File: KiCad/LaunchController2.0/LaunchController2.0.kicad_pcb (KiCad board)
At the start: 2 copper layers, 150 x 100 mm, 182 parts, among them J1 CONN_ICSP, J10 CONN_PANEL_BOARD_2, J11 CONN_AUDIO, J12 CONN_SPEAKER, J13 CONN_RS485, J2 CONN_USB, J3 USB_C_Receptacle_USB2.0_16P, J4 TO_CONVERTER, J5 FROM_CONVERTER, J6 DC_IN, J7 CONN_STATUS_PANEL, J8 CONN_BOARD_3, J9 CONN_PANEL_BOARD_1, Q1 TJ8S06M3L, Q2 2SC3325-Y, Q3 TJ8S06M3L, SW1 SW_Push, SW10 SW_Push, SW11 SW_Push, SW12 SW_Push, SW13 SW_Push, SW14 SW_Push, SW15 SW_Push, SW16 SW_Push, SW17 SW_Push, SW2 SW_Push, SW3 SW_Push, SW4 SW_Push, SW5 SW_Push, SW6 SW_Push, SW7 SW_Push, SW8 SW_Push, SW9 SW_Push, U1 ATmega2560-16A, U10 ADM2582E, U11 24LC256, U2 FT232RNL, U3 USBLC6-2SC6, U4 TPS2116DRL, U5 NJM7805SDL1, U6 INA219BIDCNT, U7 INA219BIDCNT, U9 DFPlayer, Y1 HUSG-16.000-20

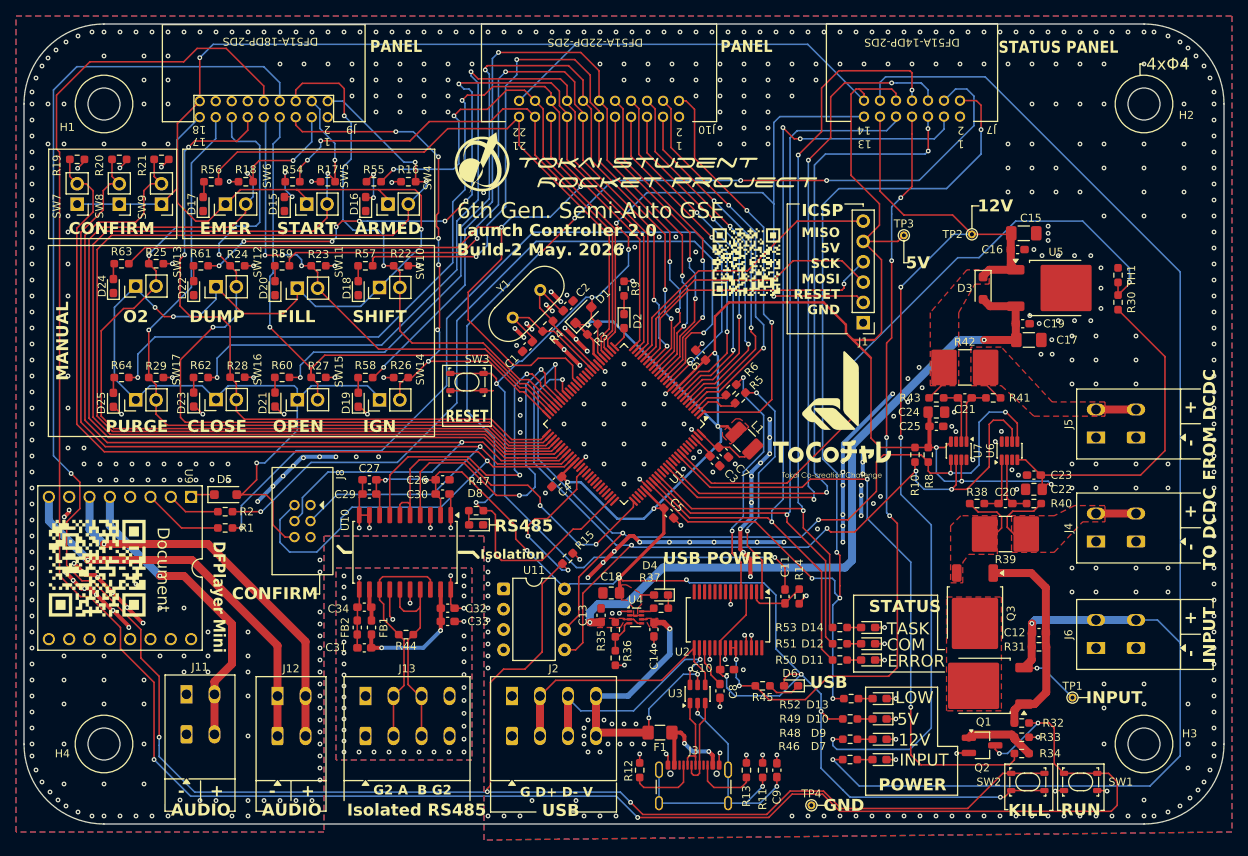
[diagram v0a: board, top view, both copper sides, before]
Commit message: シルクなどを調整
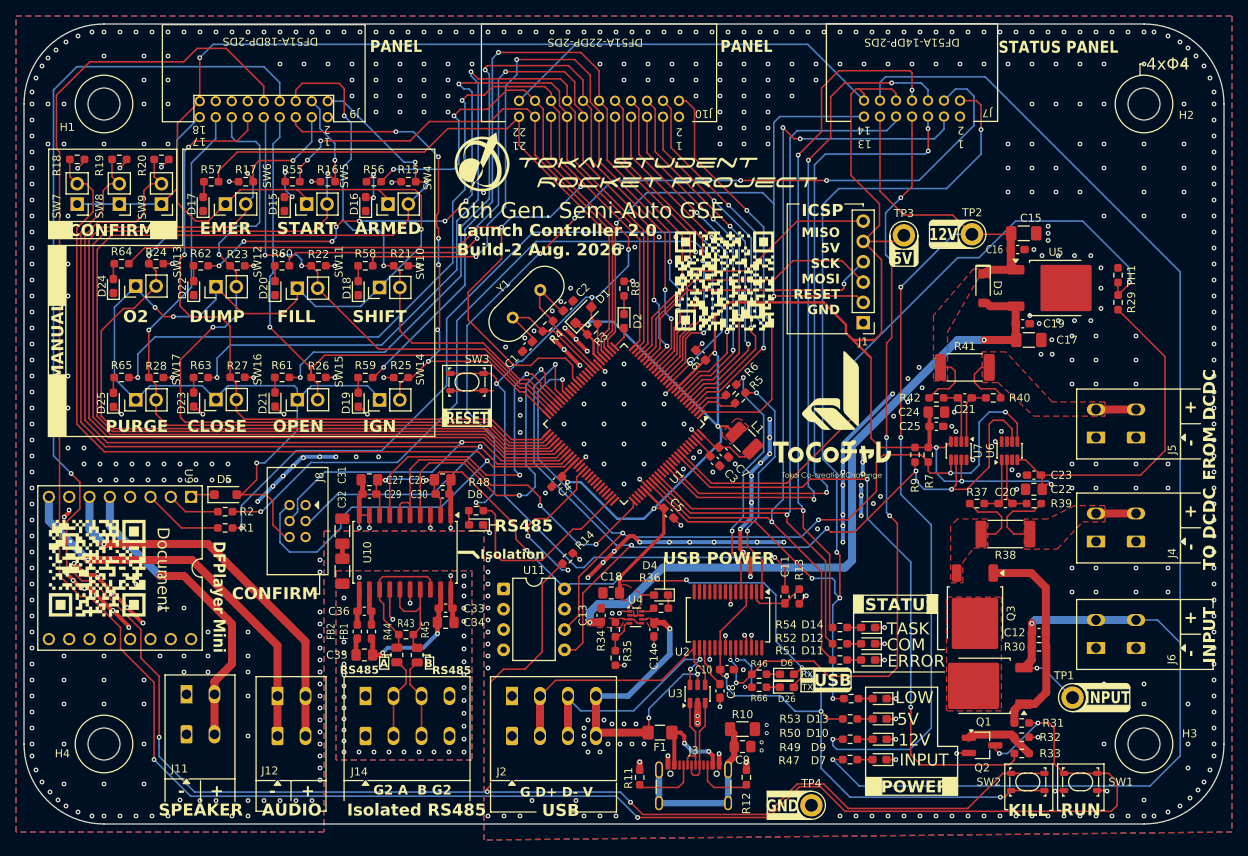
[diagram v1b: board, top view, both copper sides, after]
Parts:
- added C31: 470pF, Capacitor_SMD:C_1206_3216Metric_Pad1.33x1.80mm_HandSolder, F.Cu at (115.8, 114.4)
- added C32: 470pF, Capacitor_SMD:C_1206_3216Metric_Pad1.33x1.80mm_HandSolder, F.Cu at (115.8, 119.4)
- added D26: LED_O, LED_SMD:LED_0603_1608Metric_Pad1.05x0.95mm_HandSolder, F.Cu at (171.3, 133.9)
- added R44: TestPoint_A, Resistor_SMD:R_0805_2012Metric, F.Cu at (122.6, 129.9)
- added R45: TestPoint_B, Resistor_SMD:R_0805_2012Metric, F.Cu at (125.1, 129.9)
- added R66: 1kR, Resistor_SMD:R_0603_1608Metric_Pad0.98x0.95mm_HandSolder, F.Cu at (167.9, 133.9)
- C20, C21: value uF -> 0.1uF
- C26, C27: value 0.1uF -> 10uF; footprint Capacitor_SMD:C_0603_1608Metric_Pad1.08x0.95mm_HandSolder -> Capacitor_SMD:C_0805_2012Metric_Pad1.18x1.45mm_HandSolder
- C29, C30: value 0.01uF -> 0.1uF
- C34: renamed from C32; value 0.01uF -> 10uF; footprint Capacitor_SMD:C_0603_1608Metric_Pad1.08x0.95mm_HandSolder -> Capacitor_SMD:C_0805_2012Metric_Pad1.18x1.45mm_HandSolder
- C35: renamed from C34; value 0.01uF -> 10uF; footprint Capacitor_SMD:C_0603_1608Metric_Pad1.08x0.95mm_HandSolder -> Capacitor_SMD:C_0805_2012Metric_Pad1.18x1.45mm_HandSolder
- C9: value 4.7uF -> 10nF; footprint Capacitor_SMD:C_0603_1608Metric_Pad1.08x0.95mm_HandSolder -> Capacitor_SMD:C_0805_2012Metric_Pad1.18x1.45mm_HandSolder
- D3: value GS1010FL -> SS2040FL; footprint Diode_SMD:D_SOD-123F -> TSRP_Diode:SOD-123FL_Handsolder
- D6: value LED_B -> LED_G
- R10: renamed from R11; footprint Resistor_SMD:R_0603_1608Metric_Pad0.98x0.95mm_HandSolder -> Resistor_SMD:R_1206_3216Metric_Pad1.30x1.75mm_HandSolder
- R36: renamed from R37; value 100 -> 100R
- R37: renamed from R38; value 0R -> 10R
- R38: renamed from R39; footprint Resistor_SMD:R_2816_7142Metric_Pad3.20x4.45mm_HandSolder -> Resistor_SMD:R_2512_6332Metric_Pad1.40x3.35mm_HandSolder
- R39: renamed from R40; value 0R -> 10R
- R40: renamed from R41; value 0R -> 10R
- R41: renamed from R42; footprint Resistor_SMD:R_2816_7142Metric_Pad3.20x4.45mm_HandSolder -> Resistor_SMD:R_2512_6332Metric_Pad1.40x3.35mm_HandSolder
- R42: renamed from R43; value 0R -> 10R
- TP1, TP2, TP3, TP4: footprint TestPoint:TestPoint_THTPad_D1.0mm_Drill0.5mm -> TestPoint:TestPoint_Keystone_5005-5009_Compact
- U10: value ADM2582E -> ADM2587EBRWZ
- moved C33 11.3 mm to (128.7, 124.0), turned to 180 degrees
- moved C36 10.5 mm to (118.5, 124.4), turned to 0 degrees
- moved C35 5.97 mm to (118.5, 129.9)
- moved R10 5.72 mm to (165.8, 139.1), turned to 0 degrees
- moved C9 5.21 mm to (165.8, 141.3), turned to 180 degrees
- moved G*** 3.62 mm to (163.6, 83.1)
- moved C34 1.80 mm to (128.7, 125.8)
- moved D6 1.54 mm to (171.4, 132.3), turned to 0 degrees
- moved R46 1.51 mm to (167.9, 132.3)
- moved R11 0.91 mm to (153.0, 145.2)
- moved R12 0.91 mm to (166.3, 145.2)
- moved J8 0.61 mm to (113.8, 113.1)
- moved FB1 0.51 mm to (119.4, 126.9)
- moved FB2 0.51 mm to (117.7, 126.9)
- renumbered C31 to C33, C33 to C36, J13 to J14, R12 to R11, R13 to R12, R14 to R13, R15 to R14, R16 to R15, R17 to R16, R18 to R17, R19 to R18, R20 to R19, R21 to R20, R22 to R21, R23 to R22, R24 to R23, R25 to R24, R26 to R25, R27 to R26, R28 to R27, R29 to R28, R30 to R29, R31 to R30, R32 to R31, R33 to R32, R34 to R33, R35 to R34, R36 to R35, R44 to R43, R45 to R46, R46 to R47, R47 to R48, R48 to R49, R49 to R50, R50 to R51, R51 to R52, R52 to R53, R53 to R54, R54 to R55, R55 to R56, R56 to R57, R57 to R58, R58 to R59, R59 to R60, R60 to R61, R61 to R62, R62 to R63, R63 to R64, R64 to R65, R8 to R7, R9 to R8, R10 to R9
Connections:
- C35 pad 2: /Peripheral/Visoout -> /Peripheral/Visoin
- C36 pad 2: /Peripheral/Visoin -> /Peripheral/Visoout
- J14 pad 2: Net-(J13-Pin_2) -> Net-(J14-Pin_2)
- J14 pad 3: Net-(J13-Pin_3) -> Net-(J14-Pin_3)
- R43 pad 1: Net-(J13-Pin_3) -> Net-(U10-B)
- R43 pad 2: Net-(J13-Pin_2) -> Net-(U10-A)
- U10 pad 13: Net-(J13-Pin_2) -> Net-(U10-A)
- U10 pad 15: Net-(J13-Pin_3) -> Net-(U10-B)
- U10 pad 17: Net-(J13-Pin_3) -> Net-(U10-B)
- U10 pad 18: Net-(J13-Pin_2) -> Net-(U10-A)
- U2 pad 23: CONN_LED_USB_ACCESS -> LED_USB_TXLED
- U3 pad 2: GNDPWR -> GND
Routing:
- net Net-(J13-Pin_2): track 29.2 -> 0.00 mm
- net Net-(J13-Pin_3): track 25.0 -> 0.00 mm
- net Net-(U10-A): track 0.00 -> 17.5 mm
- net GNDPWR: track 39.1 -> 22.6 mm, vias 3 -> 0
- net Net-(U10-B): track 0.00 -> 13.1 mm
- net Net-(J14-Pin_2): track 0.00 -> 10.4 mm
- net Net-(J14-Pin_3): track 0.00 -> 10.2 mm
- net LED_USB_TXLED: track 0.00 -> 7.78 mm, vias 0 -> 2
- net FROM_CONVERTER: track 9.67 -> 12.6 mm
- net CONN_LED_12V: track 126.1 -> 128.8 mm
- net GND2: track 21.1 -> 18.4 mm, vias 40 -> 38
- net CONN_LED_5V: track 723.3 -> 725.8 mm
- net Net-(D6-K): track 4.21 -> 1.69 mm
- net GND: track 216.2 -> 214.1 mm
- net Net-(C31-Pad2): track 0.00 -> 1.88 mm
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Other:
- board text added: "A"
- board text added: "B"
- board text added: "Launch Controller 2.0 Build-2 Aug. 2026"
- board text added: "RX"
- board text added: "SPEAKER"
- board text added: "TX"
- board text removed: "Launch Controller 2.0 Build-2 May. 2026"

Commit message: BOM作成
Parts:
- D4: value LED_Y -> LED_O
- H1, H2, H3, H4: footprint MountingHole:MountingHole_4mm -> MountingHole:MountingHole_4.3mm_M4_Pad_Via
- R43: footprint Resistor_SMD:R_0603_1608Metric_Pad0.98x0.95mm_HandSolder -> Resistor_SMD:R_0805_2012Metric_Pad1.20x1.40mm_HandSolder
- U3: value USBLC6-2SC6 -> SP0504SHTG
- moved R43 0.38 mm to (123.8, 126.9)
- renumbered C29 to C28, C30 to C29, C31 to C30, C32 to C31, C33 to C32, C34 to C33, C35 to C34, C36 to C35, D8 to D10, D10 to D11, D11 to D12, D12 to D13, D13 to D14, D14 to D15, D15 to D16, D16 to D17, D17 to D18, D18 to D19, D19 to D20, D20 to D21, D21 to D22, D22 to D23, D23 to D24, D24 to D25, D25 to D26, D26 to D8, R66 to R48, R48 to R50, R50 to R51, R51 to R52, R52 to R53, R53 to R54, R54 to R55, R55 to R56, R56 to R57, R57 to R58, R58 to R59, R59 to R60, R60 to R61, R61 to R62, R62 to R63, R63 to R64, R64 to R65, R65 to R66, U11 to U10, U9 to U8, U10 to U9
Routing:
- net GND: vias 663 -> 767
